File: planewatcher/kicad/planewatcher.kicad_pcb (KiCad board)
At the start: 4 copper layers, 86.1 x 54 mm, 179 parts, among them J1 Conn_01x02, J2 RF_IN, J3 BMI-S-209-F, J4 FPGA BANK 33, J5 FPGA BANK 35 V1.2/V1.3, Q1 DMP6023LSS-13, U1 LT8608MSE, U10 AD8138ARZ, U11 AD9203ARUZ, U12 LT8640IUDCF-1#PBF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

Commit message: tidy up vias
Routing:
- net GND: vias 721 -> 797

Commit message: tidy up vias
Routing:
- net GND: vias 797 -> 783
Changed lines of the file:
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@@
 	)
 	(via
-		(at -24.41 23.88)
-		(size 0.45)
-		(drill 0.2)
-		(layers "F.Cu" "B.Cu")
-		(free yes)
-		(net "GND")
-	)
-	(via
 		(at 22.26 -18.99)
 		(size 0.45)
@@
 	)
 	(via
-		(at -15.53 19.79)
-		(size 0.45)
-		(drill 0.2)
-		(layers "F.Cu" "B.Cu")
-		(free yes)
-		(net "GND")
-	)
-	(via
 		(at -8.13 4.26)
 		(size 0.45)
@@
 	)
 	(via
-		(at 5.51 23.95)
-		(size 0.45)
-		(drill 0.2)
-		(layers "F.Cu" "B.Cu")
-		(free yes)
-		(net "GND")
-	)
-	(via
 		(at 5.59 -10.490893)
 		(size 0.45)
@@
 	)
 	(via
-		(at 25.81 23.97)
-		(size 0.45)
-		(drill 0.2)
-		(layers "F.Cu" "B.Cu")
-		(free yes)
-		(net "GND")
-	)
-	(via
 		(at -15.93 16.18)
 		(size 0.45)
@@
 	)
 	(via
-		(at -19.83 23.92)
-		(size 0.45)
-		(drill 0.2)
-		(layers "F.Cu" "B.Cu")
-		(free yes)
-		(net "GND")
-	)
-	(via
 		(at -23.89 5.85)
 		(size 0.45)
@@
 	)
 	(via
-		(at -4.72 24.07)
-		(size 0.45)
-		(drill 0.2)
-		(layers "F.Cu" "B.Cu")
-		(free yes)
-		(net "GND")
-	)
-	(via
 		(at -0.34 -12.66)
 		(size 0.45)
@@
 	)
 	(via
-		(at 20.67 24.02)
-		(size 0.45)
-		(drill 0.2)
-		(layers "F.Cu" "B.Cu")
-		(free yes)
-		(net "GND")
-	)
-	(via
 		(at 20.88 -17.06)
 		(size 0.45)
@@
 	)
 	(via
-		(at -14.88 24.01)
-		(size 0.45)
-		(drill 0.2)
-		(layers "F.Cu" "B.Cu")
-		(free yes)
-		(net "GND")
-	)
-	(via
 		(at -36.14 -13.93)
 		(size 0.45)
@@
 	)
 	(via
-		(at 10.59 24.05)
-		(size 0.45)
-		(drill 0.2)
-		(layers "F.Cu" "B.Cu")
-		(free yes)
-		(net "GND")
-	)
-	(via
 		(at -18.07 17.925)
 		(size 0.45)
@@
 	)
 	(via
-		(at 15.63 23.92)
-		(size 0.45)
-		(drill 0.2)
-		(layers "F.Cu" "B.Cu")
-		(free yes)
-		(net "GND")
-	)
-	(via
 		(at -19.82 -10.3)
 		(size 0.45)
@@
 	)
 	(via
-		(at -9.73 24.05)
-		(size 0.45)
-		(drill 0.2)
-		(layers "F.Cu" "B.Cu")
-		(free yes)
-		(net "GND")
-	)
-	(via
 		(at -29.43 -23.04)
 		(size 0.45)
@@
 	)
 	(via
-		(at 0.5 23.99)
-		(size 0.45)
-		(drill 0.2)
-		(layers "F.Cu" "B.Cu")
-		(free yes)
-		(net "GND")
-	)
-	(via
 		(at 39.82 20.324936)
 		(size 0.45)
@@
 	)
 	(via
-		(at 29.85 24.02)
-		(size 0.45)
-		(drill 0.2)
-		(layers "F.Cu" "B.Cu")
-		(free yes)
-		(net "GND")
-	)
-	(via
 		(at 28.98 -1.61)
 		(size 0.45)
@@
 		(size 0.45)
 		(drill 0.2)
-		(layers "F.Cu" "B.Cu")
-		(free yes)
-		(net "GND")
-	)
-	(via
-		(at -9.85 19.71)
-		(size 0.45)
-		(drill 0.2)

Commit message: tidy up vias
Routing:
- net GND: vias 783 -> 790
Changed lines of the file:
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@@
 	)
 	(via
+		(at 21.92 -10.89)
+		(size 0.45)
+		(drill 0.2)
+		(layers "F.Cu" "B.Cu")
+		(free yes)
+		(net "GND")
+	)
+	(via
 		(at -33.9 1.96)
 		(size 0.45)
@@
 	)
 	(via
+		(at 23.9 -9.49)
+		(size 0.45)
+		(drill 0.2)
+		(layers "F.Cu" "B.Cu")
+		(free yes)
+		(net "GND")
+	)
+	(via
 		(at -17.18 -4.76)
 		(size 0.45)
@@
 	)
 	(via
+		(at 21.65 -8.89)
+		(size 0.45)
+		(drill 0.2)
+		(layers "F.Cu" "B.Cu")
+		(free yes)
+		(net "GND")
+	)
+	(via
 		(at 3.315 17.315)
 		(size 0.45)
@@
 	)
 	(via
+		(at 20.7 -9.76)
+		(size 0.45)
+		(drill 0.2)
+		(layers "F.Cu" "B.Cu")
+		(free yes)
+		(net "GND")
+	)
+	(via
 		(at 21.81 1.07)
 		(size 0.45)
@@
 	)
 	(via
+		(at 18.58 -5.94)
+		(size 0.45)
+		(drill 0.2)
+		(layers "F.Cu" "B.Cu")
+		(free yes)
+		(net "GND")
+	)
+	(via
 		(at -24.07 17.925)
 		(size 0.45)
@@
 	)
 	(via
+		(at 25.28 -10.25)
+		(size 0.45)
+		(drill 0.2)
+		(layers "F.Cu" "B.Cu")
+		(free yes)
+		(net "GND")
+	)
+	(via
 		(at -4.63 -16.91)
 		(size 0.45)
@@
 	)
 	(via
+		(at 18.97 -15.47)
+		(size 0.45)
+		(drill 0.2)
+		(layers "F.Cu" "B.Cu")
+		(free yes)
+		(net "GND")
+	)
+	(via
 		(at -19.82 -10.3)
 		(size 0.45)
@@
 	)
 	(segment
-		(start 17.1225 -6.34)
-		(end 16.4375 -7.025)
+		(start 23.992804 -13.571232)
+		(end 23.992804 -13.162451)
 		(width 0.2)
 		(layer "F.Cu")
@@
 	)
 	(segment
-		(start 23.992804 -13.571232)
-		(end 23.992804 -13.162451)
+		(start 16.4375 -7.025)
+		(end 17.1225 -6.34)
 		(width 0.2)
 		(layer "F.Cu")
@@
 	)
 	(segment
+		(start 17.1225 -6.34)
+		(end 18.02 -6.34)
+		(width 0.2)
+		(layer "F.Cu")
+		(net "Net-(JP1-A)")
+	)
+	(segment
 		(start 21.575 -5.225)
 		(end 21.81 -5.46)
@@
 	)
 	(segment
-		(start 17.4825 -6.34)
-		(end 17.1225 -6.34)
-		(width 0.2)
-		(layer "F.Cu")
-		(net "Net-(JP1-A)")
-	)
-	(segment
 		(start 18.7675 -10.54)
 		(end 21.1325 -8.175)
@@
 	)
 	(via
-		(at 17.4825 -6.34)
+		(at 18.02 -6.34)
 		(size 0.45)
 		(drill 0.2)
@@
 	)
 	(segment
-		(start 24.0325 -11.64)
-		(end 24.0325 -13.122755)
-		(width 0.2)
-		(layer "B.Cu")
-		(net "Net-(JP1-A)")
-	)
-	(segment
-		(start 24.0325 -13.122755)
-		(end 23.992804 -13.162451)
+		(start 23.992804 -13.162451)
+		(end 23.992804 -12.142804)
 		(width 0.2)
 		(layer "B.Cu")
@@
 	)
 	(segment
-		(start 17.4825 -6.34)
-		(end 18.7325 -6.34)
+		(start 18.19 -6.34)
+		(end 18.02 -6.34)
 		(width 0.2)
 		(layer "B.Cu")
@@
 	)
 	(segment
-		(start 18.7325 -6.34)
-		(end 24.0325 -11.64)
+		(start 23.992804 -12.142804)
+		(end 18.19 -6.34)
 		(width 0.2)
 		(layer "B.Cu")

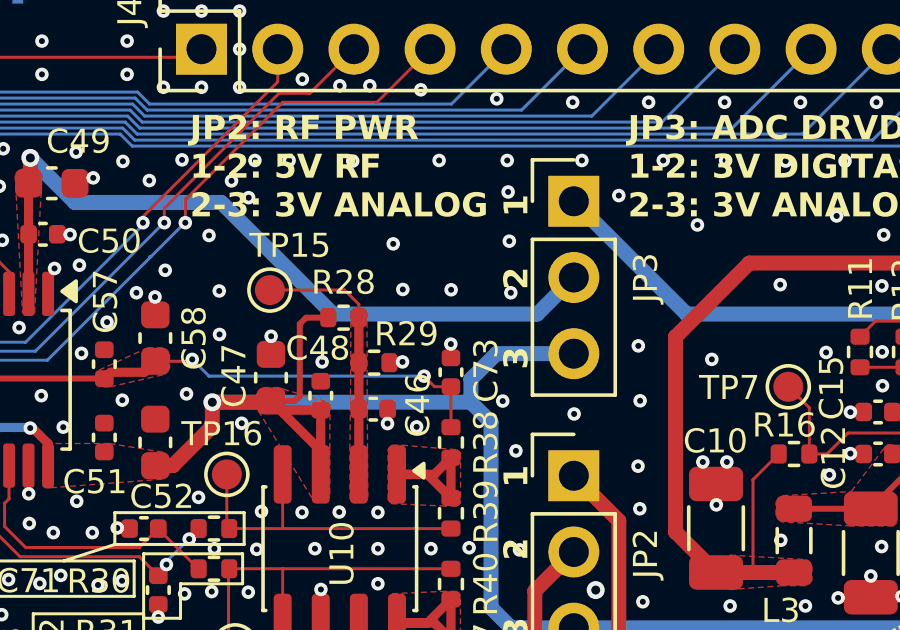
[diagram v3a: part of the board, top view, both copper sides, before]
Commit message: add test point for ADC VREF
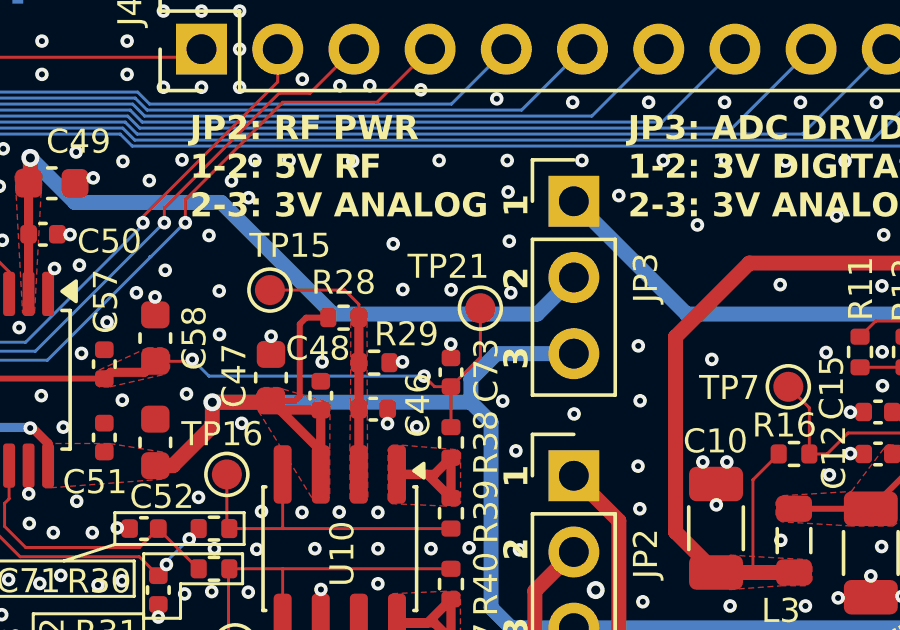
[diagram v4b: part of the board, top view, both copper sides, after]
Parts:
- added TP21: VREF, TestPoint:TestPoint_Pad_D1.0mm, F.Cu at (-11.9, -14.1)
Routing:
- net /ADC/VREF: track 21.1 -> 24.1 mm
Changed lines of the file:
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@@
 		)
 	)
+	(footprint "TestPoint:TestPoint_Pad_D1.0mm"
+		(layer "F.Cu")
+		(at -11.865 -14.135)
+		(descr "SMD pad as test Point, diameter 1.0mm")
+		(tags "test point SMD pad")
+		(property "Reference" "TP21"
+			(at -1.065 -1.385 0)
+			(layer "F.SilkS" knockout)
+			(effects
+				(font
+					(size 0.8 0.8)
+					(thickness 0.15)
+				)
+			)
+		)
+		(property "Value" "VREF"
+			(at 0 1.55 0)
+			(layer "F.Fab")
+			(effects
+				(font
+					(size 1 1)
+					(thickness 0.15)
+				)
+			)
+		)
+		(property "Datasheet" ""
+			(at 0 0 0)
+			(unlocked yes)
+			(layer "F.Fab")
+			(hide yes)
+			(effects
+				(font
+					(size 1.27 1.27)
+					(thickness 0.15)
+				)
+			)
+		)
+		(property "Description" "test point"
+			(at 0 0 0)
+			(unlocked yes)
+			(layer "F.Fab")
+			(hide yes)
+			(effects
+				(font
+					(size 1.27 1.27)
+					(thickness 0.15)
+				)
+			)
+		)
+		(property ki_fp_filters "Pin* Test*")
+		(sheetname "/ADC/")
+		(sheetfile "ADC.kicad_sch")
+		(units
+			(unit
+				(name "A")
+				(pins "1")
+			)
+		)
+		(duplicate_pad_numbers_are_jumpers no)
+		(fp_circle
+			(center 0 0)
+			(end 0 0.7)
+			(stroke
+				(width 0.12)
+				(type solid)
+			)
+			(fill no)
+			(layer "F.SilkS")
+		)
+		(fp_circle
+			(center 0 0)
+			(end 1 0)
+			(stroke
+				(width 0.05)
+				(type solid)
+			)
+			(fill no)
+			(layer "F.CrtYd")
+		)
+		(fp_text user "${REFERENCE}"
+			(at 0 -1.45 0)
+			(layer "F.Fab")
+			(effects
+				(font
+					(size 1 1)
+					(thickness 0.15)
+				)
+			)
+		)
+		(pad "1" smd circle
+			(at 0 0)
+			(size 1 1)
+			(layers "F.Cu" "F.Mask")
+			(net "/ADC/VREF")
+			(pinfunction "1_1")
+			(pintype "passive")
+		)
+		(embedded_fonts no)
+	)
 	(footprint "Capacitor_SMD:C_1210_3225Metric"
 		(layer "F.Cu")
@@
 		(sheetname "/RF_Input_Protection/")
 		(sheetfile "RF_Input_Protection.kicad_sch")
+		(units
+			(unit
+				(name "A")
+				(pins "1" "2")
+			)
+		)
 		(attr smd)
 		(duplicate_pad_numbers_are_jumpers no)
@@
 	)
 	(segment
+		(start -11.865 -12.5)
+		(end -11.865 -14.135)
+		(width 0.1)
+		(layer "F.Cu")
+		(net "/ADC/VREF")
+	)
+	(segment
 		(start -24.19 -12)
 		(end -23.065 -12)
@@
 		(width 0.1)
 		(layer "F.Cu")
+		(net "/ADC/VREF")
+	)
+	(segment
+		(start -12.845 -11.52)
+		(end -11.865 -12.5)
+		(width 0.1)
+		(layer "F.Cu")

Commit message: updates before fab
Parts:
- added FID1: Fiducial_1mm_Mask2mm, Fiducial:Fiducial_1mm_Mask2mm, F.Cu at (-34.0, 25.2)
- added FID2: Fiducial_1mm_Mask2mm, Fiducial:Fiducial_1mm_Mask2mm, F.Cu at (34.0, -25.2)
- added FID3: Fiducial_1mm_Mask2mm, Fiducial:Fiducial_1mm_Mask2mm, F.Cu at (34.0, 25.2)
- added MH1: MountingHole_3.5mm_Pad_Via, MountingHole:MountingHole_3.5mm_Pad_Via, F.Cu at (-38.6, 22.5)
- added MH2: MountingHole_3.5mm_Pad_Via, MountingHole:MountingHole_3.5mm_Pad_Via, F.Cu at (38.6, 22.5)
- added MH3: MountingHole_3.5mm_Pad_Via, MountingHole:MountingHole_3.5mm_Pad_Via, F.Cu at (38.6, -22.5)
- added MH4: MountingHole_3.5mm_Pad_Via, MountingHole:MountingHole_3.5mm_Pad_Via, F.Cu at (-38.6, -22.5)
- D3: value ESD112-B1-02ELS -> ESD103-B1-02EL
- F1: value Bourns MF-MSMF200/24X 2.0A -> Littelfuse 1812L300/24SLER 3.0A
- L2, L4, L6: value 2.2µH -> 4.7µH
- moved J4 0.05 mm to (-21.2, -22.7)
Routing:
- net /FPGA_U22: track 29.6 -> 33.4 mm, vias 0 -> 2
- net GND: vias 790 -> 728
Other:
- outline, holes or cut-outs redrawn
